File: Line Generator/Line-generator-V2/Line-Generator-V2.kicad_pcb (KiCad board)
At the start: 2 copper layers, 41 x 29.2 mm, 24 parts, among them J1 Conn_01x04, Q1 BS170F, Q2 BCP5310, Q3 BCP5310, Q4 BS170F, U1 TLC272

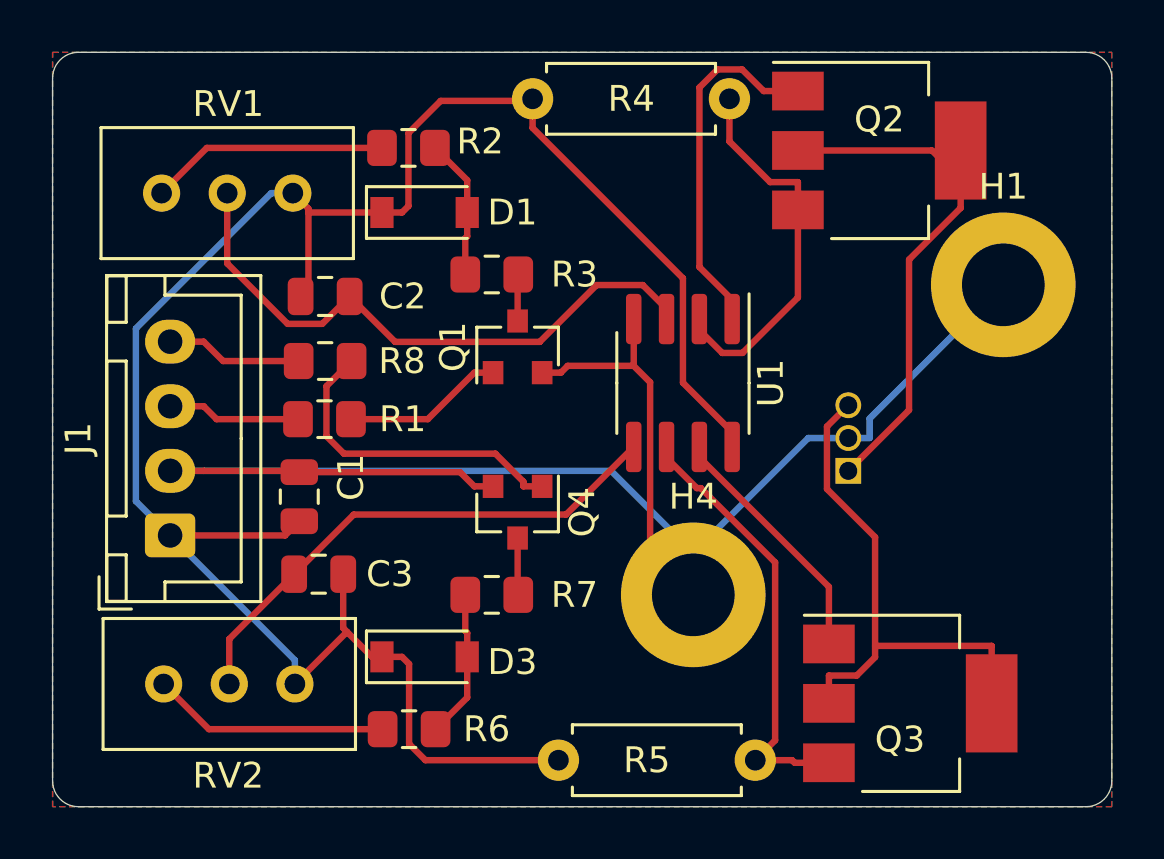
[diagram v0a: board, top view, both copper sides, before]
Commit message: Updated PCB layout
Added vias to improve soldering
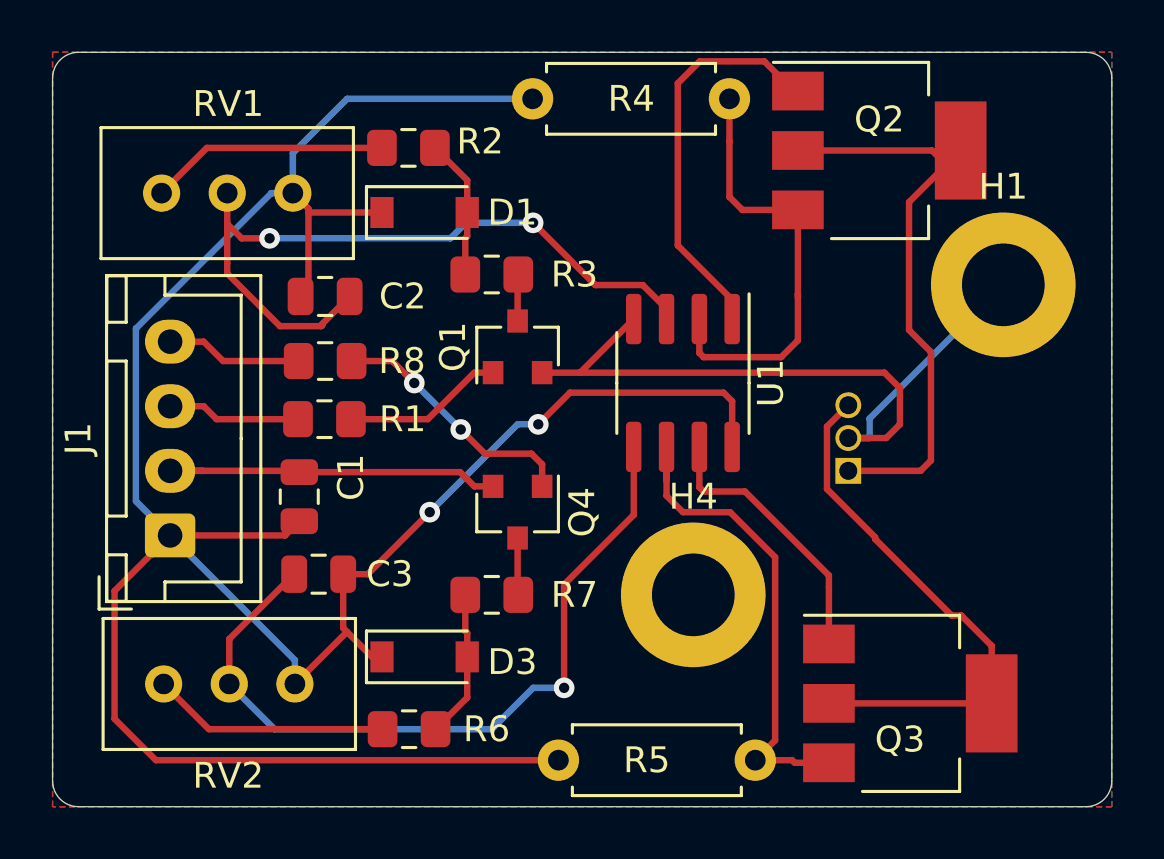
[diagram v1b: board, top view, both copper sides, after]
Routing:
- net +5V: track 80.1 -> 102.0 mm, vias 0 -> 2
- net GND: track 68.0 -> 47.6 mm
- net Net-(C3-Pad2): track 20.5 -> 30.1 mm, vias 0 -> 1
- net Net-(C2-Pad2): track 23.6 -> 28.5 mm, vias 0 -> 2
- net Net-(D2-Pad1): track 21.0 -> 24.4 mm
- net Net-(Q2-Pad3): track 14.9 -> 17.7 mm
- net Net-(Q4-Pad1): track 12.6 -> 9.88 mm, vias 0 -> 2
- net Net-(Q3-Pad3): track 17.2 -> 19.4 mm
- net Net-(Q2-Pad1): track 13.9 -> 15.5 mm
- net Net-(Q3-Pad1): track 9.70 -> 11.0 mm

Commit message: Updated PCB layout as per AB suggestion
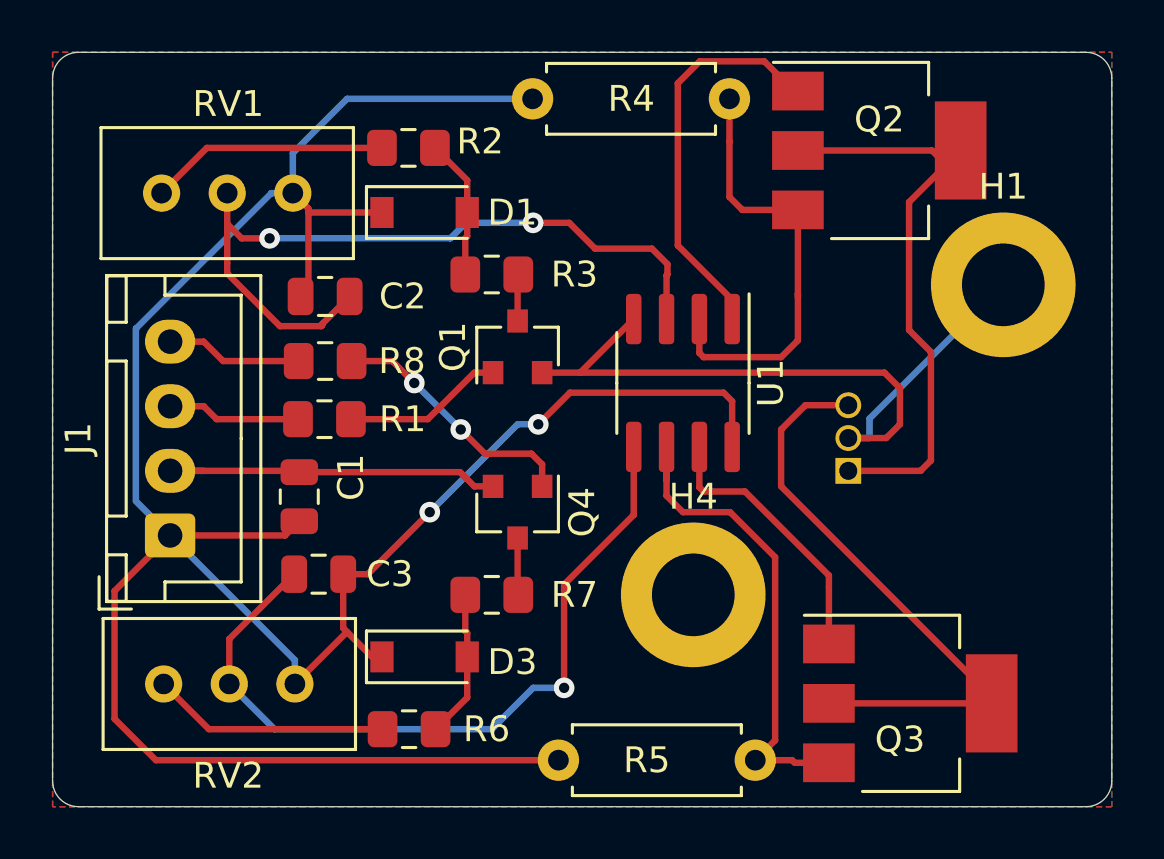
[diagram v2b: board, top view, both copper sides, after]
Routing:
- net Net-(D2-Pad3): track 21.0 -> 23.3 mm
- net Net-(C2-Pad2): track 28.5 -> 29.9 mm
